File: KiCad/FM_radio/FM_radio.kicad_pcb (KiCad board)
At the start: 2 copper layers, 33 x 48 mm, 75 parts, among them IC1 TPA741DR, IC2 SI4703-C19-GM, IC3 TPA6111A2DR, IC4 MCP73831T-2ACI_OT, J3 Conn_01x06_Pin, J4 SJ2-35853A-SMT-TR, J5 UJC-HP2-3-SMT-TR, U3 ATmega328P-A, Y2 ABS06N-32.768kHz-T

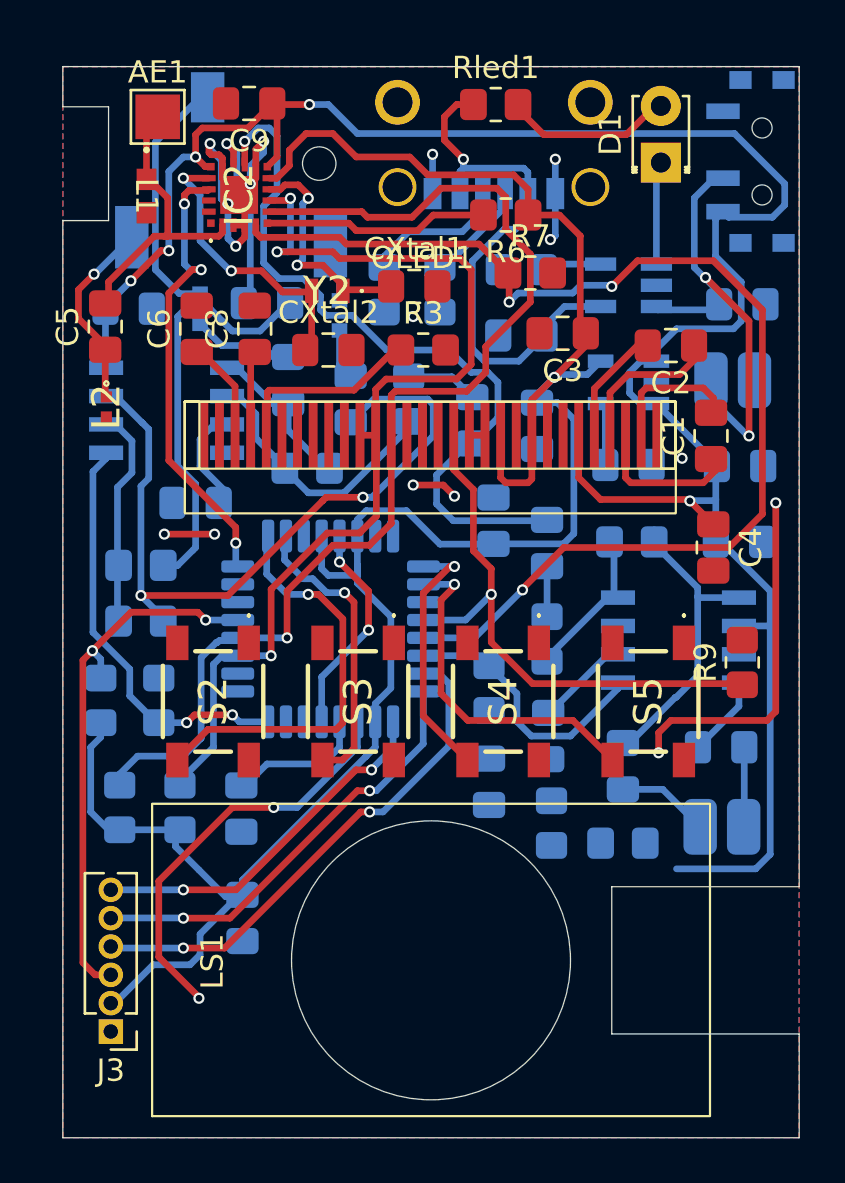
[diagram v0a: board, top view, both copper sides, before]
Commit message: Consultation update
Before removing hole in PCB for speaker
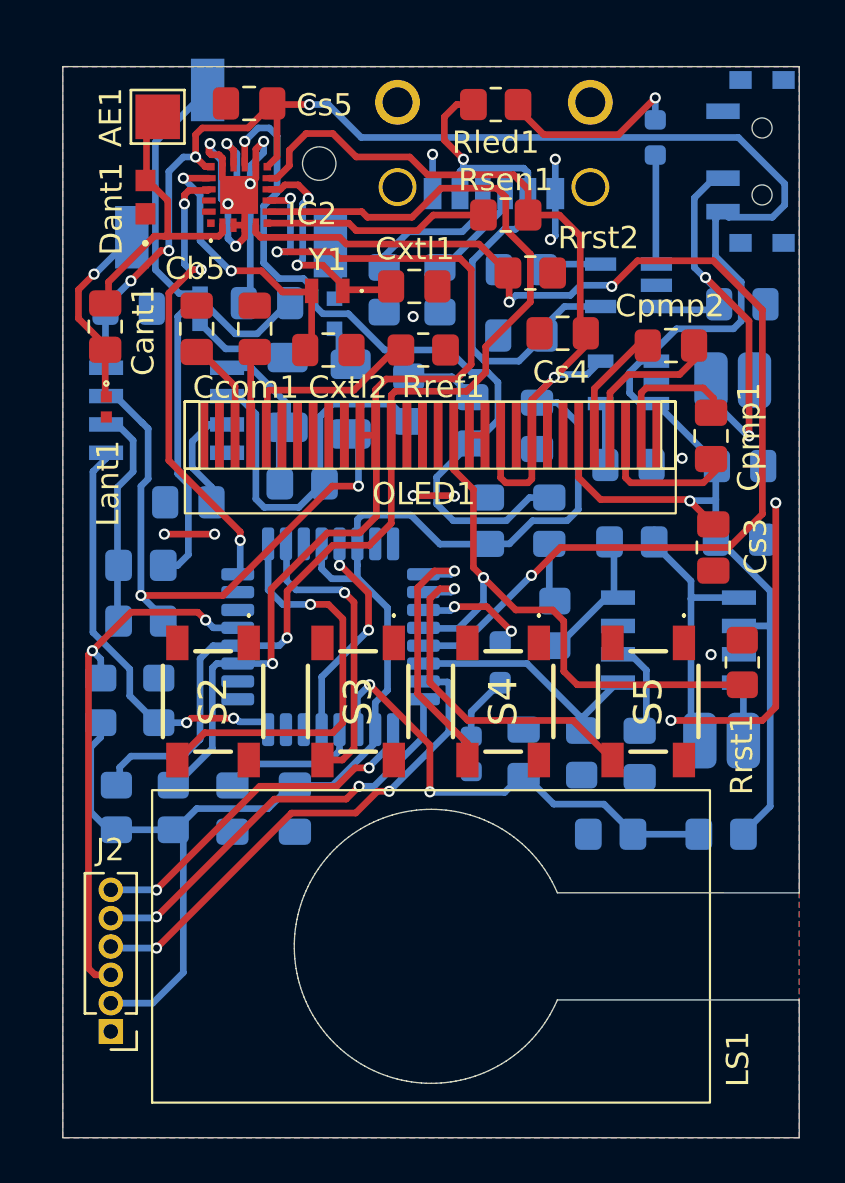
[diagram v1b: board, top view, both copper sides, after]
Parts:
- removed CC1, CC2: 47u, Capacitor_SMD:C_0805_2012Metric_Pad1.18x1.45mm_HandSolder
- removed L1: PGB1010603MR, Footprints:IND_PGB_0603_LTF
- added D2: LED, LED_SMD:LED_0603_1608Metric, B.Cu at (138.3, 100.8)
- added Dant1: PGB1010603MR, Footprints:IND_PGB_0603_LTF, F.Cu at (123.7, 75.8)
- added Rled2: 1k, Resistor_SMD:R_0603_1608Metric_Pad0.98x0.95mm_HandSolder, B.Cu at (139.6, 96.7)
- Cc1: renamed from CC6; footprint Capacitor_SMD:C_0805_2012Metric_Pad1.18x1.45mm_HandSolder -> Capacitor_SMD:C_1206_3216Metric_Pad1.33x1.80mm_HandSolder
- Cc2: renamed from CC7; footprint Capacitor_SMD:C_0805_2012Metric_Pad1.18x1.45mm_HandSolder -> Capacitor_SMD:C_1206_3216Metric_Pad1.33x1.80mm_HandSolder
- Cxtl1: renamed from CXtal1; value 12p5 -> 22p
- Cxtl2: renamed from CXtal2; value 12p5 -> 22p
- D1: footprint LED_THT:LED_D1.8mm_W3.3mm_H2.4mm -> LED_SMD:LED_0603_1608Metric; moved to B.Cu
- moved FB1 6.26 mm to (126.2, 80.8)
- moved FB2 6.03 mm to (132.2, 81.1), turned to -90 degrees
- moved Cs2 5.43 mm to (130.4, 103.2)
- moved Rsd1 5.06 mm to (143.2, 100.8)
- moved Rd1 4.42 mm to (149.5, 104.4)
- moved Cb4 4.18 mm to (145.8, 100.8)
- moved Rd2 2.70 mm to (144.6, 104.4), turned to 180 degrees
- moved Cb3 2.02 mm to (140.7, 100.8), turned to 90 degrees
- moved D1 1.15 mm to (146.6, 73.2)
- moved Cin3 1.00 mm to (141.8, 90.3)
- moved Rin1 0.78 mm to (142.1, 95.0)
- moved Rfb2 0.74 mm to (130.7, 88.7), turned to 0 degrees
- moved LS1 0.61 mm to (136.5, 109.4)
- moved Cc1 0.55 mm to (130.1, 84.6)
- moved Cb2 0.40 mm to (127.6, 103.2)
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- renumbered C5 to Cant1, Cbyp1 to Cb1, CB6 to Cb2, CB7 to Cb3, CB2 to Cb4, C6 to Cb5, CB4 to Cb6, CB5 to Cb7, C8 to Ccom1, CI1 to Cin3, CI2 to Cin4, CI3 to Cin5, C1 to Cpmp1, C2 to Cpmp2, CB1 to Cs1, CB3 to Cs2, C4 to Cs3, C3 to Cs4, C9 to Cs5, Cs1 to Cs6, IC4 to IC1, IC1 to IC3, IC3 to IC4, J5 to J1, J3 to J2, J4 to J3, L2 to Lant1, Rcc3 to Rcc1, Rcc4 to Rcc2, R5 to Rclk1, R12 to Rd1, R13 to Rd2, RF1 to Rfb1, RF4 to Rfb2, RF2 to Rfb3, RI1 to Rin1, RI2 to Rin2, RI3 to Rin3, Rprog1 to Rprg1, R3 to Rref1, R8 to Rrst0, R9 to Rrst1, R7 to Rrst2, R10 to Rsd1, R11 to Rsd2, R4 to Rsda1, R6 to Rsen1, U3 to U1, Y2 to Y1
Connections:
- Cc1 pad 1: Net-(CC6-Pad1) -> Net-(Cc1-Pad1)
- Cc2 pad 1: Net-(IC3-VO2) -> Net-(Cc2-Pad1)
- Cc2 pad 2: Net-(CC7-Pad2) -> Net-(IC4-VO2)
- FB1 pad 1: Net-(CC7-Pad2) -> Net-(Cc1-Pad1)
- FB1 pad 2: Net-(J4-TIP) -> Net-(J3-RING)
- FB2 pad 1: Net-(CC6-Pad1) -> Net-(J3-TIP)
- FB2 pad 2: Net-(J4-RING) -> Net-(Cc2-Pad1)
- IC3 pad 5: Net-(IC1-VO+) -> Net-(IC3-VO+)
- IC3 pad 8: Net-(IC1-VO-) -> Net-(IC3-VO-)
- IC4 pad 7: Net-(IC3-VO2) -> Net-(IC4-VO2)
- J3 pad 2: Net-(J4-TIP) -> Net-(J3-TIP)
- J3 pad 3: Net-(J4-RING) -> Net-(J3-RING)
- LS1 pad 1: Net-(CC1-Pad1) -> Net-(IC3-VO-)
- LS1 pad 2: Net-(CC2-Pad1) -> Net-(IC3-VO+)
- Rfb1 pad 2: Net-(IC1-VO+) -> Net-(IC3-VO+)
- Rfb3 pad 1: Net-(IC3-VO2) -> Net-(IC4-VO2)
- U1 pad 11: unconnected-(U3-PD7-Pad11) -> Net-(U1-PD7)
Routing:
- net Net-(IC3-VO2): track 33.9 -> 0.00 mm, vias 2 -> 0
- net Net-(IC4-VO2): track 0.00 -> 26.4 mm, vias 0 -> 2
- net Net-(IC1-VO+): track 13.8 -> 0.00 mm
- net Net-(IC3-VO+): track 0.00 -> 13.1 mm
- net Net-(J4-RING): track 11.5 -> 0.00 mm
- net Net-(J3-RING): track 0.00 -> 11.5 mm
- net Net-(U1-PD7): track 0.00 -> 5.21 mm, vias 0 -> 2
- net /Vbat: track 101.7 -> 96.8 mm
- net Net-(IC4-IN1-): track 12.1 -> 16.9 mm
- net Net-(CC6-Pad1): track 4.57 -> 0.00 mm
- net Net-(Cc1-Pad1): track 0.00 -> 4.55 mm
- net Net-(CC2-Pad1): track 4.16 -> 0.00 mm
- net Net-(IC1-VO-): track 3.66 -> 0.00 mm
- net Net-(CC1-Pad1): track 3.58 -> 0.00 mm
- net Net-(IC3-VO-): track 0.00 -> 3.29 mm
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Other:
- outline, holes or cut-outs redrawn

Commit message: Speaker on TOP of PCB
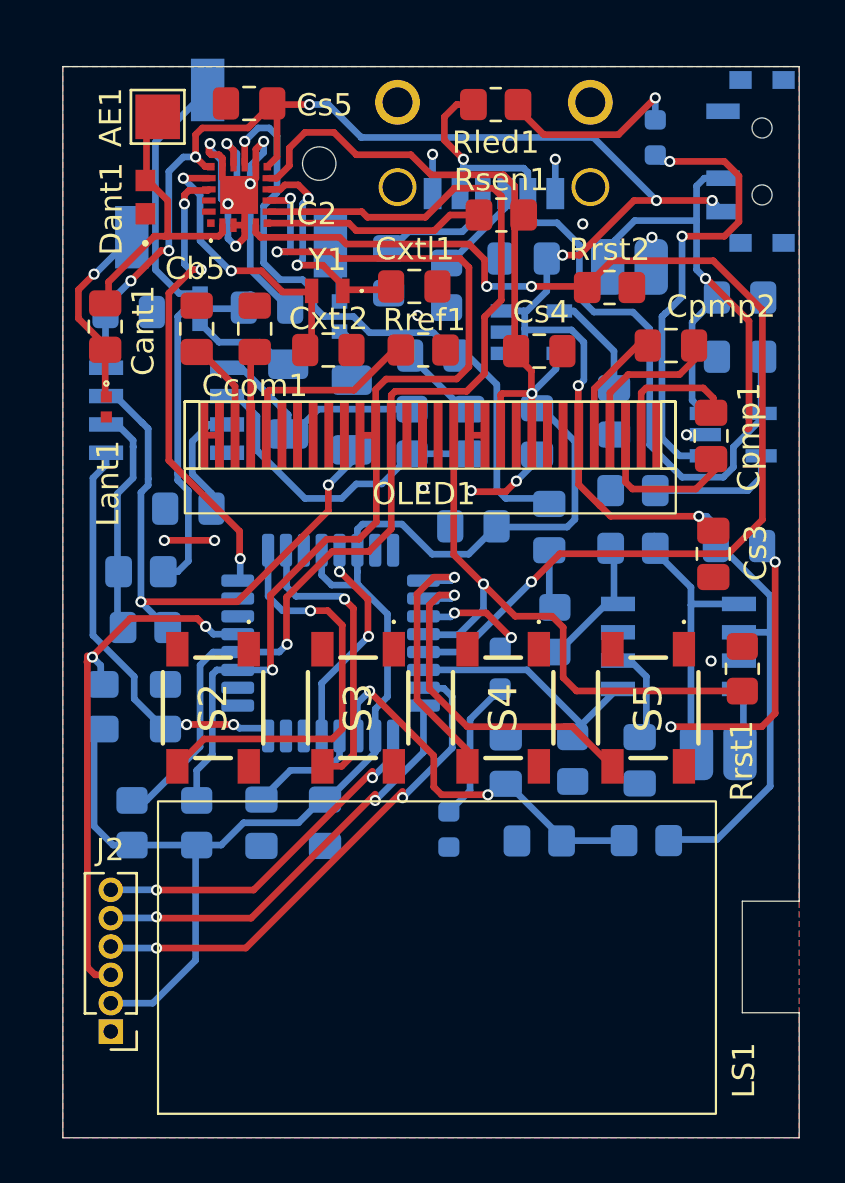
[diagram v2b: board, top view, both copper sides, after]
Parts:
- added kibuzzard-69A389EF: G***, kibuzzard-69A389EF, B.Cu at (131.9, 115.3)
- added kibuzzard-69A38A54: G***, kibuzzard-69A38A54, B.Cu at (142.3, 115.3)
- moved Cin2 13.4 mm to (140.7, 78.6), turned to 0 degrees
- moved Rprg1 11.1 mm to (145.6, 89.0)
- moved Cin1 9.85 mm to (150.3, 83.0)
- moved IC1 8.17 mm to (150.0, 86.5), turned to 0 degrees
- moved Rfb2 5.46 mm to (135.7, 86.3), turned to -90 degrees
- moved PS1 4.90 mm to (141.0, 81.9), turned to 0 degrees
- moved Rrst2 3.61 mm to (144.5, 79.9)
- moved D2 3.53 mm to (137.3, 104.2)
- moved Cin4 3.39 mm to (136.6, 83.0), turned to 180 degrees
- moved Rd1 3.36 mm to (146.2, 104.7)
- moved Rd2 3.21 mm to (141.3, 104.7)
- moved Rin2 3.06 mm to (138.2, 86.3)
- moved Cb1 2.49 mm to (144.7, 85.5), turned to 90 degrees
- moved Cs2 1.49 mm to (131.7, 103.9)
- moved Cb2 1.45 mm to (128.9, 103.9)
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- renumbered Cb7 to Cs7
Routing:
- net Net-(D1-K): track 4.88 -> 20.7 mm, vias 0 -> 2
- net Net-(IC1-VDD): track 24.8 -> 34.5 mm
- net /3v3: track 99.3 -> 92.8 mm
- net Net-(BT1-+): track 21.1 -> 26.3 mm, vias 2 -> 1
- net /ROUT: track 34.3 -> 29.3 mm
- net /Vbat: track 96.8 -> 92.9 mm, vias 5 -> 9
- net /ADC: track 21.3 -> 17.4 mm
- net Net-(IC4-VO1): track 7.78 -> 11.4 mm
- net Net-(D2-A): track 2.94 -> 6.45 mm
- net Net-(IC1-PROG): track 2.65 -> 5.96 mm
- net Net-(IC4-IN1-): track 16.9 -> 14.5 mm
- net Net-(PS1-BYP/ADJ/NC): track 2.84 -> 4.86 mm
- net /SCL: track 51.9 -> 50.1 mm
- net GND: track 50.6 -> 48.9 mm, vias 19 -> 21
- net Net-(Cin5-Pad2): track 18.9 -> 17.3 mm
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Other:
- outline, holes or cut-outs redrawn

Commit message: JLC constraints
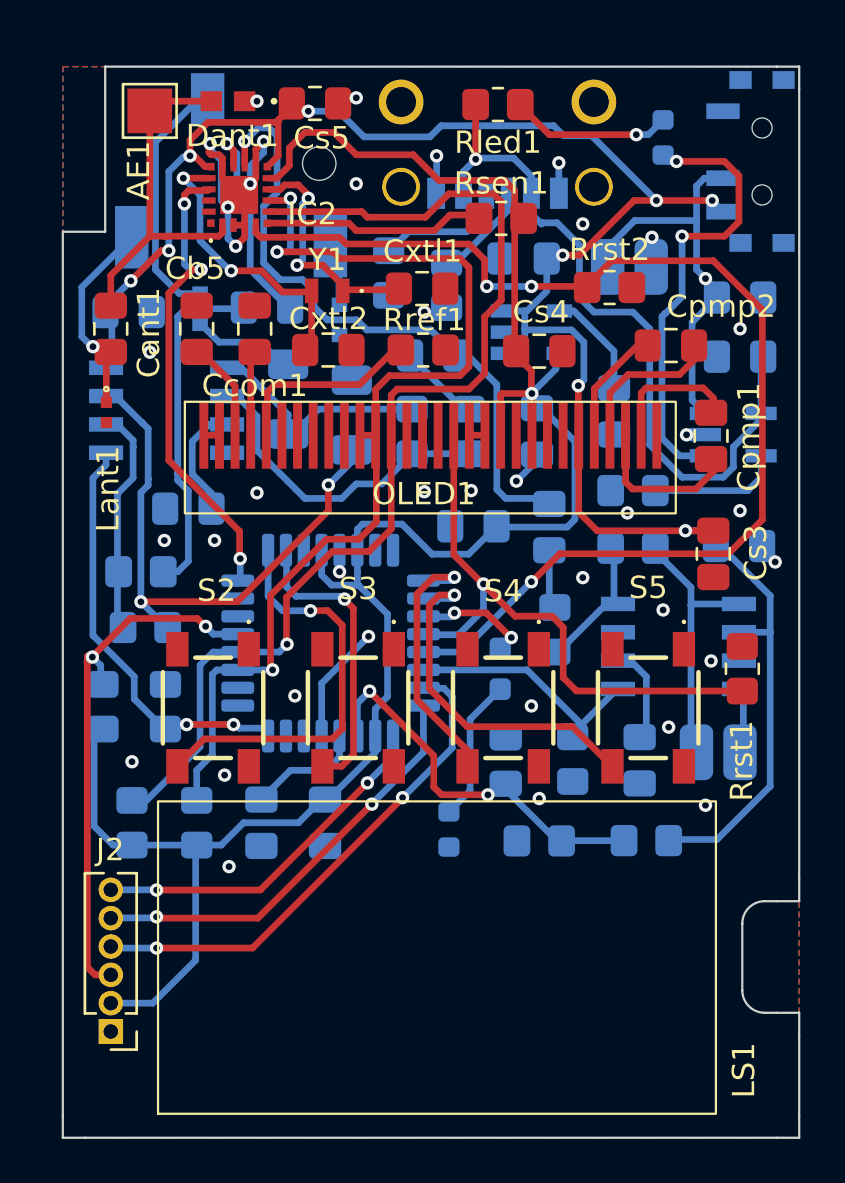
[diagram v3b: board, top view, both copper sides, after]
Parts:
- moved Dant1 5.67 mm to (127.4, 71.5), turned to 180 degrees
- moved Cs5 2.95 mm to (131.3, 71.7), turned to 0 degrees
- moved AE1 0.44 mm to (123.9, 72.0)
- moved Cxtl1 0.36 mm to (136.1, 80.0)
- moved D1 0.35 mm to (146.9, 73.2)
- moved Cant1 0.27 mm to (122.2, 81.8)
- moved Lant1 0.25 mm to (122.0, 85.5)
- moved J1 0.16 mm to (139.5, 72.4)
- moved FB2 0.15 mm to (132.4, 81.3)
- moved Rsen1 0.15 mm to (139.7, 76.8)
- moved Rcc2 0.10 mm to (134.6, 79.2)
- moved Rled1 0.10 mm to (139.5, 71.7)
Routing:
- net GND: track 48.9 -> 30.0 mm, vias 21 -> 38
- net Net-(BT1-+): track 26.3 -> 18.7 mm
- net /ANT: track 13.6 -> 16.2 mm
- net Net-(IC1-VDD): track 34.5 -> 33.0 mm
- net Net-(D1-A): track 8.52 -> 7.43 mm
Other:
- outline, holes or cut-outs redrawn

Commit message: Editing footprints
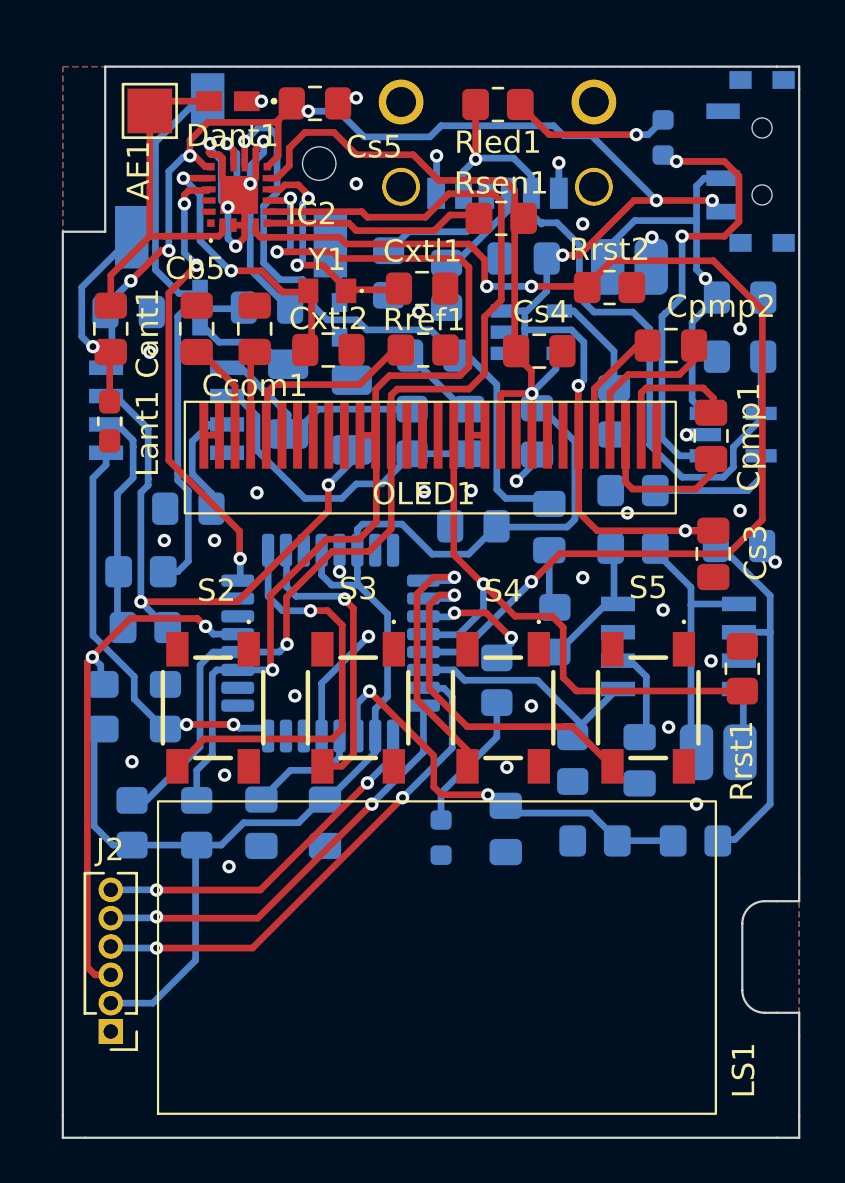
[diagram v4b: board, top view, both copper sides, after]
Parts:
- Lant1: footprint Footprints:MLG1005 -> Inductor_SMD:L_0603_1608Metric_Pad1.05x0.95mm_HandSolder
- Rled2: footprint Resistor_SMD:R_0603_1608Metric_Pad0.98x0.95mm_HandSolder -> Resistor_SMD:R_0805_2012Metric_Pad1.20x1.40mm_HandSolder
- moved Cb3 3.06 mm to (139.8, 104.2), turned to -90 degrees
- moved Rd2 2.50 mm to (143.8, 104.7)
- moved Rd1 2.20 mm to (148.3, 104.7)
- moved kibuzzard-69A389EF 0.67 mm to (131.9, 114.6)
- moved kibuzzard-69A38A54 0.67 mm to (142.3, 114.6)
- moved Rled2 0.54 mm to (139.4, 97.5)
- moved D2 0.51 mm to (136.9, 104.5)
- moved Lant1 0.43 mm to (122.1, 85.9)
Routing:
- net /Vbat: track 92.9 -> 91.2 mm
- net /GPIO2: track 21.3 -> 20.6 mm
- net Net-(J3-SLEEVE): track 8.72 -> 8.16 mm
- net /SD1: track 10.9 -> 11.4 mm
